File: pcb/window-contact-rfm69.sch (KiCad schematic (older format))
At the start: 23 parts, among them IC1 ATMEGA328P-A, P1 VCC, P2 TX/RX, P3 RE1, P4 ISP, P5 RE2, P6 AN

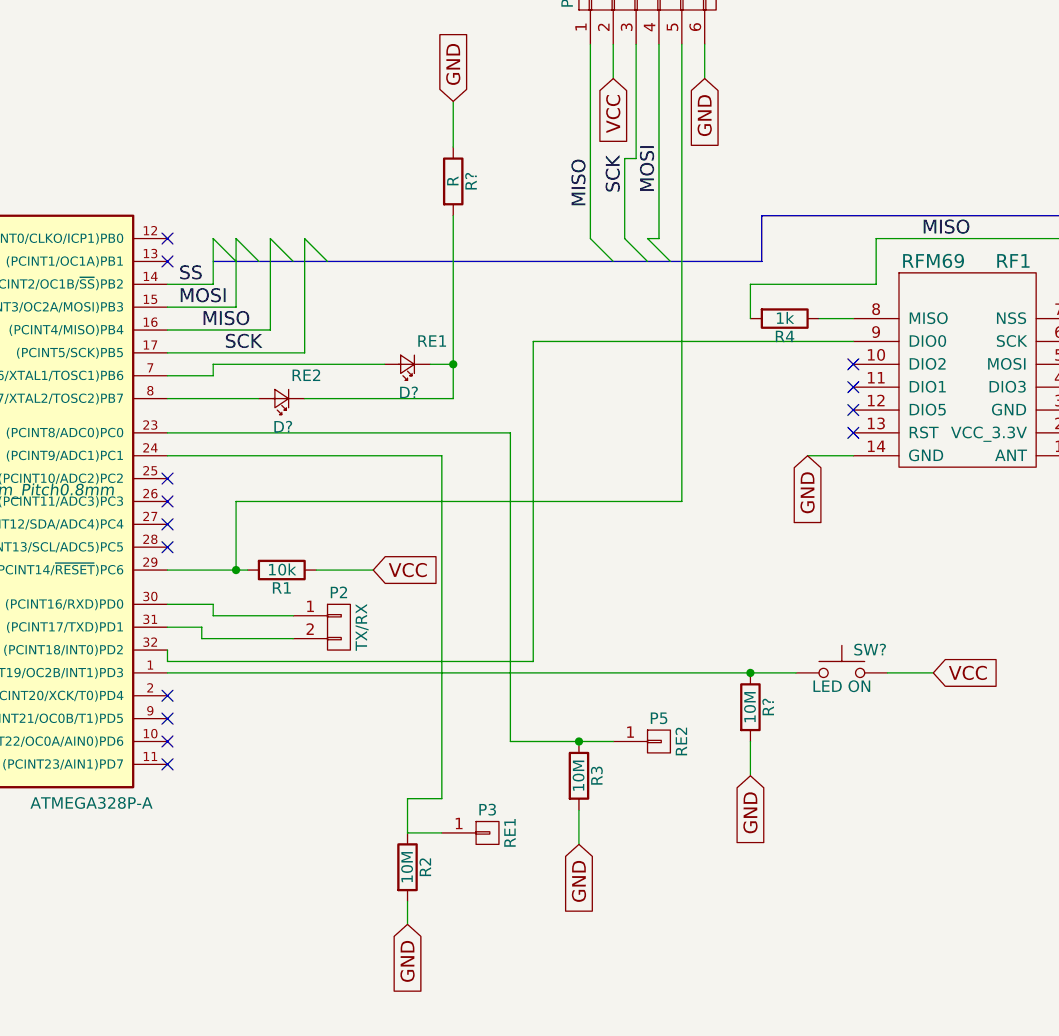
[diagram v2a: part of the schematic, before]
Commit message: added 3. reed contact
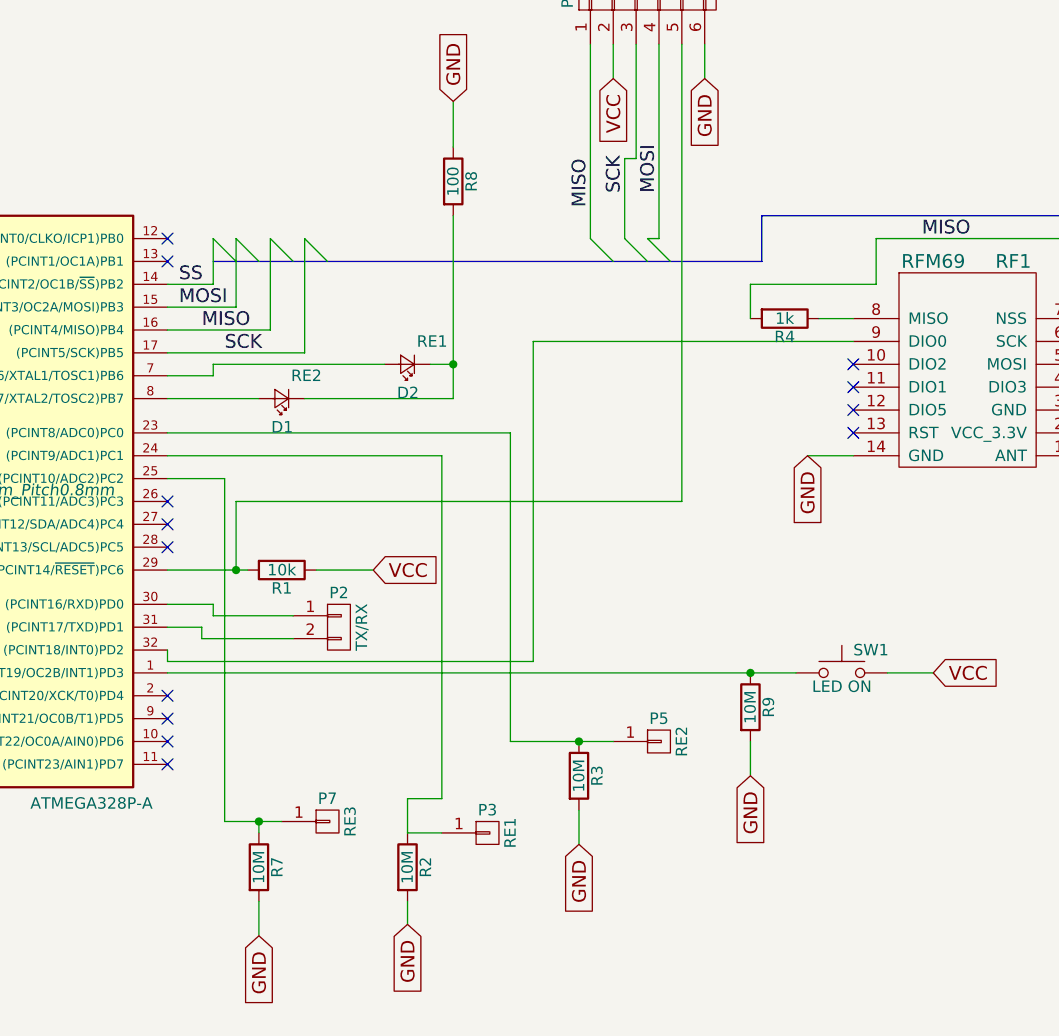
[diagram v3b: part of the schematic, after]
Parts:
- added P7: RE3, wirepad:Wire_SMD_Pad_1PIN, symbol CONN_01X01
- added R7: 10M, Resistors_SMD:R_0805_HandSoldering, symbol R
- R8: renamed from R?; value R -> 100
- gave numbers to parts that had none: 4
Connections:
- net GND: now also R7.2
- net at IC1.25 ((PCINT10/ADC2)PC2): now also P7.1 (P1), R7.1
- no-connect marks 18 -> 17
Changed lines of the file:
@@
 NoConn ~ 4200 4450
 NoConn ~ 4200 4550
-NoConn ~ 4200 5500
 NoConn ~ 4200 5600
 NoConn ~ 4200 5700
@@
 NoConn ~ 4200 6750
 $Comp
-L CONN_01X02 P2
-U 1 1 5B19964F
-P 4950 6150
-F 0 "P2" H 4950 6300 50  0000 C CNN
-F 1 "TX/RX" V 5050 6150 50  0000 C CNN
-F 2 "Pin_Headers:Pin_Header_Straight_1x02" H 4950 6150 50  0001 C CNN
-F 3 "" H 4950 6150 50  0000 C CNN
-	1    4950 6150
-	1    0    0    -1
-$EndComp
-Wire Wire Line
-	4750 6100 4400 6100
-Wire Wire Line
-	4400 6100 4400 6050
-Wire Wire Line
-	4400 6050 4200 6050
-Wire Wire Line
-	4200 6150 4350 6150
-Wire Wire Line
-	4350 6150 4350 6200
-Wire Wire Line
-	4350 6200 4750 6200
-$Comp
-L R R?
+L R R9
 U 1 1 5B891AA9
 P 6750 6500
-F 0 "R?" V 6830 6500 50  0000 C CNN
+F 0 "R9" V 6830 6500 50  0000 C CNN
 F 1 "10M" V 6750 6500 50  0000 C CNN
 F 2 "Resistors_SMD:R_0805_HandSoldering" V 6680 6500 50  0001 C CNN
@@
 	6750 6650 6750 6800
 $Comp
-L SW_Push SW?
+L SW_Push SW1
 U 1 1 5B8920C1
 P 7150 6350
-F 0 "SW?" H 7200 6450 50  0000 L CNN
+F 0 "SW1" H 7200 6450 50  0000 L CNN
 F 1 "LED ON" H 7150 6290 50  0000 C CNN
 F 2 "" H 7150 6550 50  0001 C CNN
@@
 Connection ~ 6750 6350
 $Comp
-L R R?
+L R R8
 U 1 1 5B892B3A
 P 5450 4200
-F 0 "R?" V 5530 4200 50  0000 C CNN
-F 1 "R" V 5450 4200 50  0000 C CNN
-F 2 "" V 5380 4200 50  0000 C CNN
+F 0 "R8" V 5530 4200 50  0000 C CNN
+F 1 "100" V 5450 4200 50  0000 C CNN
+F 2 "" V 5380 4200 50  0001 C CNN
 F 3 "" H 5450 4200 50  0000 C CNN
 	1    5450 4200
@@
 	5450 3850 5450 4050
 $Comp
-L LED_Small D?
+L LED_Small D2
 U 1 1 5B892EF0
 P 5250 5000
-F 0 "D?" H 5200 5125 50  0000 L CNN
+F 0 "D2" H 5200 5125 50  0000 L CNN
 F 1 "RE1" H 5075 4900 50  0000 L CNN
-F 2 "" V 5250 5000 50  0000 C CNN
+F 2 "" V 5250 5000 50  0001 C CNN
 F 3 "" V 5250 5000 50  0000 C CNN
 	1    5250 5000
@@
 $EndComp
 $Comp
-L LED_Small D?
+L LED_Small D1
 U 1 1 5B8932F8
 P 4700 5150
-F 0 "D?" H 4650 5275 50  0000 L CNN
+F 0 "D1" H 4650 5275 50  0000 L CNN
 F 1 "RE2" H 4525 5050 50  0000 L CNN
-F 2 "" V 4700 5150 50  0000 C CNN
+F 2 "" V 4700 5150 50  0001 C CNN
 F 3 "" V 4700 5150 50  0000 C CNN
 	1    4700 5150
@@
 Wire Wire Line
 	5450 5000 5350 5000
+Wire Wire Line
+	4350 6150 4350 6200
+Wire Wire Line
+	4350 6200 4750 6200
+Wire Wire Line
+	4200 6150 4350 6150
+Wire Wire Line
+	4400 6050 4200 6050
+Wire Wire Line
+	4400 6100 4400 6050
+Wire Wire Line
+	4750 6100 4400 6100
+$Comp
+L CONN_01X02 P2
+U 1 1 5B19964F
+P 4950 6150
+F 0 "P2" H 4950 6300 50  0000 C CNN
+F 1 "TX/RX" V 5050 6150 50  0000 C CNN
+F 2 "Pin_Headers:Pin_Header_Straight_1x02" H 4950 6150 50  0001 C CNN
+F 3 "" H 4950 6150 50  0000 C CNN
+	1    4950 6150
+	1    0    0    -1
+$EndComp
+Text GLabel 4600 7500 3    60   Input ~ 0
+GND
+$Comp
+L R R7
+U 1 1 5B91A3F9
+P 4600 7200
+F 0 "R7" V 4680 7200 50  0000 C CNN
+F 1 "10M" V 4600 7200 50  0000 C CNN
+F 2 "Resistors_SMD:R_0805_HandSoldering" V 4530 7200 50  0001 C CNN
+F 3 "" H 4600 7200 50  0000 C CNN
+	1    4600 7200
+	1    0    0    -1
+$EndComp
+$Comp
+L CONN_01X01 P7
+U 1 1 5B91A4BB
+P 4900 7000
+F 0 "P7" H 4900 7100 50  0000 C CNN
+F 1 "RE3" V 5000 7000 50  0000 C CNN
+F 2 "wirepad:Wire_SMD_Pad_1PIN" H 4900 7000 50  0001 C CNN
+F 3 "" H 4900 7000 50  0000 C CNN
+	1    4900 7000
+	1    0    0    -1
+$EndComp
+Wire Wire Line
+	4200 5500 4450 5500
+Wire Wire Line
+	4450 5500 4450 7000
+Wire Wire Line
+	4450 7000 4700 7000
+Wire Wire Line
+	4600 7000 4600 7050
+Connection ~ 4600 7000
+Wire Wire Line
+	4600 7350 4600 7500
 $EndSCHEMATC

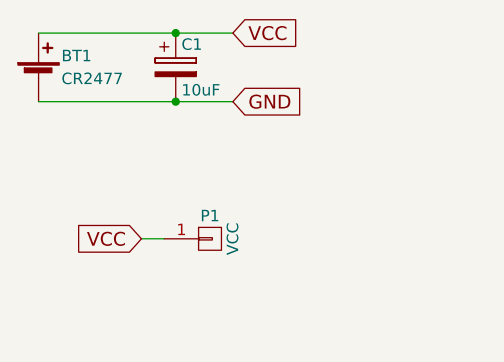
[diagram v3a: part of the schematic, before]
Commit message: new release of pcb for window four state contact
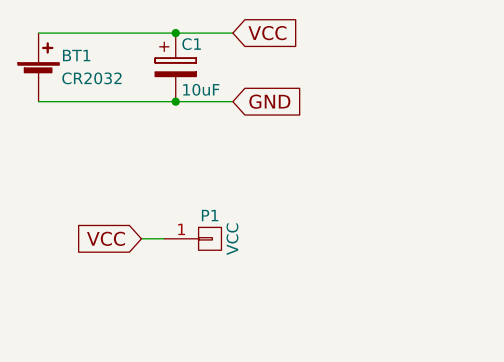
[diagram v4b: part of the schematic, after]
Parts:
- BT1: value CR2477 -> CR2032; footprint battery:CR2477 -> battery:CR2032
- D1, D2: footprint (none) -> LEDs:LED_0805
- P6: footprint Wire_Pads:SolderWirePad_single_1mmDrill -> wirepad:Wire_SMD_Pad_1PIN
- R8: footprint (none) -> Resistors_SMD:R_0805_HandSoldering
- SW1: footprint (none) -> button:SMD_Button
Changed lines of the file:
@@
 P 1050 1400
 F 0 "BT1" H 1150 1500 50  0000 L CNN
-F 1 "CR2477" H 1150 1400 50  0000 L CNN
-F 2 "battery:CR2477" V 1050 1460 50  0001 C CNN
+F 1 "CR2032" H 1150 1400 50  0000 L CNN
+F 2 "battery:CR2032" V 1050 1460 50  0001 C CNN
 F 3 "" V 1050 1460 50  0000 C CNN
 	1    1050 1400
@@
 F 0 "P6" H 8600 5700 50  0000 C CNN
 F 1 "AN" V 8700 5600 50  0000 C CNN
-F 2 "Wire_Pads:SolderWirePad_single_1mmDrill" H 8600 5600 50  0001 C CNN
+F 2 "wirepad:Wire_SMD_Pad_1PIN" H 8600 5600 50  0001 C CNN
 F 3 "" H 8600 5600 50  0000 C CNN
 	1    8600 5600
@@
 F 0 "SW1" H 7200 6450 50  0000 L CNN
 F 1 "LED ON" H 7150 6290 50  0000 C CNN
-F 2 "" H 7150 6550 50  0001 C CNN
+F 2 "button:SMD_Button" H 7150 6550 50  0001 C CNN
 F 3 "" H 7150 6550 50  0001 C CNN
 	1    7150 6350
@@
 F 0 "R8" V 5530 4200 50  0000 C CNN
 F 1 "100" V 5450 4200 50  0000 C CNN
-F 2 "" V 5380 4200 50  0001 C CNN
+F 2 "Resistors_SMD:R_0805_HandSoldering" V 5380 4200 50  0001 C CNN
 F 3 "" H 5450 4200 50  0000 C CNN
 	1    5450 4200
@@
 F 0 "D2" H 5200 5125 50  0000 L CNN
 F 1 "RE1" H 5075 4900 50  0000 L CNN
-F 2 "" V 5250 5000 50  0001 C CNN
+F 2 "LEDs:LED_0805" V 5250 5000 50  0001 C CNN
 F 3 "" V 5250 5000 50  0000 C CNN
 	1    5250 5000
@@
 F 0 "D1" H 4650 5275 50  0000 L CNN
 F 1 "RE2" H 4525 5050 50  0000 L CNN
-F 2 "" V 4700 5150 50  0001 C CNN
+F 2 "LEDs:LED_0805" V 4700 5150 50  0001 C CNN
 F 3 "" V 4700 5150 50  0000 C CNN
 	1    4700 5150

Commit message: updated pcb
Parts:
- BT1: symbol Battery_Cell -> window-contact-rfm69-rescue:Battery_Cell
- C1: symbol CP -> window-contact-rfm69-rescue:CP
- C2, C3: symbol C -> window-contact-rfm69-rescue:C
- D1, D2: symbol LED_Small -> window-contact-rfm69-rescue:LED_Small
- IC1: symbol ATMEGA328P-A -> window-contact-rfm69-rescue:ATMEGA328P-A
- P1, P3, P5, P6, P7: symbol CONN_01X01 -> window-contact-rfm69-rescue:CONN_01X01
- P2: symbol CONN_01X02 -> window-contact-rfm69-rescue:CONN_01X02
- P4: symbol CONN_01X06 -> window-contact-rfm69-rescue:CONN_01X06
- R1, R2, R3, R4, R5, R6, R7, R8, R9: symbol R -> window-contact-rfm69-rescue:R
- RF1: symbol RFM69 -> rfm69:RFM69
- SW1: symbol SW_Push -> Switch1:SW_Push
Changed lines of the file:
@@
-EESchema Schematic File Version 2
-LIBS:power
-LIBS:device
-LIBS:transistors
-LIBS:conn
-LIBS:linear
-LIBS:regul
-LIBS:74xx
-LIBS:cmos4000
-LIBS:adc-dac
-LIBS:memory
-LIBS:xilinx
-LIBS:microcontrollers
-LIBS:dsp
-LIBS:microchip
-LIBS:analog_switches
-LIBS:motorola
-LIBS:texas
-LIBS:intel
-LIBS:audio
-LIBS:interface
-LIBS:digital-audio
-LIBS:philips
-LIBS:display
-LIBS:cypress
-LIBS:siliconi
-LIBS:opto
-LIBS:atmel
-LIBS:contrib
-LIBS:valves
-LIBS:rfm69
-LIBS:Switch
+EESchema Schematic File Version 4
 LIBS:window-contact-rfm69-cache
-EELAYER 25 0
+EELAYER 26 0
 EELAYER END
 $Descr A4 11693 8268
@@
 $EndDescr
 $Comp
-L Battery_Cell BT1
+L window-contact-rfm69-rescue:Battery_Cell BT1
 U 1 1 5B016578
 P 1050 1400
@@
 $EndComp
 $Comp
-L C C3
+L window-contact-rfm69-rescue:C C3
 U 1 1 5B016625
 P 2100 5150
@@
 $EndComp
 $Comp
-L R R2
+L window-contact-rfm69-rescue:R R2
 U 1 1 5B01665D
 P 5250 7200
@@
 $EndComp
 $Comp
-L R R1
+L window-contact-rfm69-rescue:R R1
 U 1 1 5B0166FD
 P 4700 5900
@@
 VCC
 $Comp
-L CP C1
+L window-contact-rfm69-rescue:CP C1
 U 1 1 5B018A0C
 P 1650 1350
@@
 $EndComp
 Wire Wire Line
-	1050 1500 1900 1500
+	1050 1500 1650 1500
 Connection ~ 1650 1500
 Wire Wire Line
-	1050 1200 1900 1200
+	1050 1200 1650 1200
 Connection ~ 1650 1200
 $Comp
-L ATMEGA328P-A IC1
+L window-contact-rfm69-rescue:ATMEGA328P-A IC1
 U 1 1 5B0ACB62
 P 3200 5550
@@
 NoConn ~ 2300 5050
 $Comp
-L C C2
+L window-contact-rfm69-rescue:C C2
 U 1 1 5B13F6B2
 P 2000 4650
@@
 VCC
 Wire Wire Line
-	1750 4500 2300 4500
-Wire Wire Line
-	2300 4450 2300 4550
+	1750 4500 2000 4500
+Wire Wire Line
+	2300 4450 2300 4500
 Connection ~ 2000 4500
 Connection ~ 2300 4500
 Wire Wire Line
-	2000 4800 2000 6900
+	2000 4800 2000 6650
 Wire Wire Line
 	2000 6650 2300 6650
@@
 	2300 5000 2300 4750
 Wire Wire Line
-	1800 5000 2300 5000
+	1800 5000 2100 5000
 Connection ~ 2100 5000
 Wire Wire Line
 	2100 5300 2100 6550
 Wire Wire Line
-	2100 6550 2300 6550
+	2100 6550 2200 6550
 Text GLabel 2200 6900 3    60   Input ~ 0
 GND
@@
 NoConn ~ 2300 5900
 $Comp
-L R R6
+L window-contact-rfm69-rescue:R R6
 U 1 1 5B140033
 P 8800 5000
@@
 $EndComp
 $Comp
-L RFM69 RF1
+L rfm69:RFM69 RF1
 U 1 1 5B1401F8
 P 7600 5100
@@
 	5100 5900 4850 5900
 Wire Wire Line
-	4550 5900 4200 5900
+	4550 5900 4500 5900
 Text GLabel 8600 5300 2    60   Input ~ 0
 VCC
@@
 	8200 5200 8950 5200
 $Comp
-L CONN_01X01 P6
+L window-contact-rfm69-rescue:CONN_01X01 P6
 U 1 1 5B140A1B
 P 8600 5600
@@
 NoConn ~ 7200 5100
 $Comp
-L R R5
+L window-contact-rfm69-rescue:R R5
 U 1 1 5B140CDD
 P 8500 4900
@@
 $EndComp
 $Comp
-L R R4
+L window-contact-rfm69-rescue:R R4
 U 1 1 5B140D43
 P 6900 4800
@@
 	8200 5000 8650 5000
 Wire Bus Line
-	4400 4550 6800 4550
-Wire Bus Line
 	6800 4550 6800 4350
 Wire Bus Line
-	6800 4350 8300 4350
-Wire Bus Line
 	8300 4350 8300 4400
 Entry Wire Line
@@
 Wire Wire Line
 	4400 4650 4200 4650
-Wire Wire Line
-	4500 4450 4500 4750
 Wire Wire Line
 	4500 4750 4200 4750
@@
 MOSI
 $Comp
-L CONN_01X06 P4
+L window-contact-rfm69-rescue:CONN_01X06 P4
 U 1 1 5B19650E
 P 6300 3400
@@
 MOSI
 $Comp
-L CONN_01X01 P5
+L window-contact-rfm69-rescue:CONN_01X01 P5
 U 1 1 5B197BA2
 P 6350 6650
@@
 $EndComp
 $Comp
-L CONN_01X01 P3
+L window-contact-rfm69-rescue:CONN_01X01 P3
 U 1 1 5B197C31
 P 5600 7050
@@
 $EndComp
 $Comp
-L CONN_01X01 P1
+L window-contact-rfm69-rescue:CONN_01X01 P1
 U 1 1 5B197CCB
 P 1800 2100
@@
 	1600 2100 1500 2100
 $Comp
-L R R3
+L window-contact-rfm69-rescue:R R3
 U 1 1 5B1981B6
 P 6000 6800
@@
 	6000 7100 6000 6950
 Wire Wire Line
-	5700 6650 6150 6650
+	5700 6650 6000 6650
 Wire Wire Line
 	4200 5300 5700 5300
@@
 NoConn ~ 4200 6750
 $Comp
-L R R9
+L window-contact-rfm69-rescue:R R9
 U 1 1 5B891AA9
 P 6750 6500
@@
 GND
 Wire Wire Line
-	4200 6350 6950 6350
+	4200 6350 6750 6350
 Wire Wire Line
 	6750 6650 6750 6800
 $Comp
-L SW_Push SW1
+L Switch1:SW_Push SW1
 U 1 1 5B8920C1
 P 7150 6350
@@
 Connection ~ 6750 6350
 $Comp
-L R R8
+L window-contact-rfm69-rescue:R R8
 U 1 1 5B892B3A
 P 5450 4200
@@
 	5450 3850 5450 4050
 $Comp
-L LED_Small D2
+L window-contact-rfm69-rescue:LED_Small D2
 U 1 1 5B892EF0
 P 5250 5000
@@
 $EndComp
 $Comp
-L LED_Small D1
+L window-contact-rfm69-rescue:LED_Small D1
 U 1 1 5B8932F8
 P 4700 5150
@@
 Connection ~ 5450 5000
 Wire Wire Line
-	5450 4350 5450 5150
+	5450 4350 5450 5000
 Wire Wire Line
 	5450 5000 5350 5000
@@
 	4750 6100 4400 6100
 $Comp
-L CONN_01X02 P2
+L window-contact-rfm69-rescue:CONN_01X02 P2
 U 1 1 5B19964F
 P 4950 6150
@@
 GND
 $Comp
-L R R7
+L window-contact-rfm69-rescue:R R7
 U 1 1 5B91A3F9
 P 4600 7200
@@
 $EndComp
 $Comp
-L CONN_01X01 P7
+L window-contact-rfm69-rescue:CONN_01X01 P7
 U 1 1 5B91A4BB
 P 4900 7000
@@
 	4450 5500 4450 7000
 Wire Wire Line
-	4450 7000 4700 7000
+	4450 7000 4600 7000
 Wire Wire Line
 	4600 7000 4600 7050
@@
 Wire Wire Line
 	4600 7350 4600 7500
+Wire Wire Line
+	1650 1500 1900 1500
+Wire Wire Line
+	1650 1200 1900 1200
+Wire Wire Line
+	2000 4500 2300 4500
+Wire Wire Line
+	2300 4500 2300 4550
+Wire Wire Line
+	2000 6650 2000 6750
+Wire Wire Line
+	2000 6750 2000 6900
+Wire Wire Line
+	2100 5000 2300 5000
+Wire Wire Line
+	2200 6550 2300 6550
+Wire Wire Line
+	4500 5900 4200 5900
+Wire Wire Line
+	6000 6650 6150 6650
+Wire Wire Line
+	6750 6350 6950 6350
+Wire Wire Line
+	5450 5000 5450 5150
+Wire Wire Line
+	4600 7000 4700 7000
+Wire Wire Line
+	4500 4450 4500 4750
+Wire Bus Line
+	6800 4350 8300 4350
+Wire Bus Line
+	4400 4550 6800 4550
 $EndSCHEMATC
